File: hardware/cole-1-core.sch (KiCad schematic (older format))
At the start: 11 parts, among them SW1 SW_Push, U1 WD65C02, U2 ECS-100AX-2.0, U3 MAX1232CPA, U4 AT28C256-15PU, U5 CY62256NLL-70PXC

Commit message: - Change WE on the EEPROM to be tied to ground, like it is on the breadboard prototype. - Change TD pin on the MAX1232 to bre tied to Vcc, which raises the watchdog timeout to 1.2s. - Add Vcc and GND pins to each of the GPIO headers
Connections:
- wire segments 119 -> 121
- no-connect marks 7 -> 6
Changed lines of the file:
@@
 	9250 2150 9450 2150
-Wire Wire Line
-	4850 5150 9800 5150
 Wire Wire Line
 	4750 5250 9800 5250
@@
 	9800 800  9800 2200
 Wire Wire Line
-	5050 2750 4850 2750
-Wire Wire Line
-	4850 2750 4850 5150
+	4400 2750 5050 2750
 Wire Wire Line
 	4750 5250 4750 2850
@@
 Wire Wire Line
 	9450 2150 9450 5150
-Connection ~ 9450 5150
 Wire Wire Line
 	9250 2050 9350 2050
@@
 	4800 5550 4800 7000
 Connection ~ 3600 7000
-NoConn ~ 1850 7000
 Entry Wire Line
 	2700 2700 2800 2600
@@
 Entry Wire Line
 	2700 2300 2800 2200
+$Comp
+L VCC #PWR05
+U 1 1 5A514B68
+P 1700 6650
+F 0 "#PWR05" H 1700 6500 50  0001 C CNN
+F 1 "VCC" H 1700 6800 50  0000 C CNN
+F 2 "" H 1700 6650 50  0001 C CNN
+F 3 "" H 1700 6650 50  0001 C CNN
+	1    1700 6650
+	1    0    0    -1
+$EndComp
+Wire Wire Line
+	1850 7000 1700 7000
+Wire Wire Line
+	1700 7000 1700 6650
+$Comp
+L VCC #PWR06
+U 1 1 5A514D73
+P 4400 2400
+F 0 "#PWR06" H 4400 2250 50  0001 C CNN
+F 1 "VCC" H 4400 2550 50  0000 C CNN
+F 2 "" H 4400 2400 50  0001 C CNN
+F 3 "" H 4400 2400 50  0001 C CNN
+	1    4400 2400
+	1    0    0    -1
+$EndComp
+Wire Wire Line
+	4400 2400 4400 2750
+Wire Wire Line
+	9450 5150 9800 5150
 $EndSCHEMATC

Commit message: switch to a DIP-8 oscillator, and fix footprint for MAX1232
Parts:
- U2: value ECS-100AX-2.0 -> ECS-2100AX-2.0MHZ; footprint Housings_DIP:DIP-14_W7.62mm_Socket_LongPads -> Housings_DIP:DIP-8_W7.62mm_Socket_LongPads; symbol Osc_14pin -> Osc_8pin
- U3: footprint Housings_DIP:DIP-14_W7.62mm_Socket_LongPads -> Housings_DIP:DIP-8_W7.62mm_Socket_LongPads
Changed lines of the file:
@@
 F 0 "U3" H 2450 7350 60  0000 L BNN
 F 1 "MAX1232CPA" H 2200 6700 60  0000 L BNN
-F 2 "Housings_DIP:DIP-14_W7.62mm_Socket_LongPads" H 2600 7900 50  0001 L BNN
+F 2 "Housings_DIP:DIP-8_W7.62mm_Socket_LongPads" H 2600 7900 50  0001 L BNN
 F 3 "Maxim Integrated" H 2750 8100 50  0001 L BNN
 	1    2500 7050
@@
 	2700 2800 2700 5050
 $Comp
-L Osc_14pin U2
+L Osc_8pin U2
 U 1 1 5A43653F
 P 1900 4150
 F 0 "U2" H 1900 4450 60  0000 C CNN
-F 1 "ECS-100AX-2.0" H 1950 3850 60  0000 C CNN
-F 2 "Housings_DIP:DIP-14_W7.62mm_Socket_LongPads" H 1900 4150 60  0001 C CNN
+F 1 "ECS-2100AX-2.0MHZ" H 1950 3850 60  0000 C CNN
+F 2 "Housings_DIP:DIP-8_W7.62mm_Socket_LongPads" H 1900 4150 60  0001 C CNN
 F 3 "" H 1900 4150 60  0001 C CNN
 	1    1900 4150

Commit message: Final schematic and PCB layout.
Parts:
- R1, R2, R3, R4, R6: footprint Resistors_THT:R_Axial_DIN0207_L6.3mm_D2.5mm_P10.16mm_Horizontal -> Resistors_SMD:R_0805_HandSoldering
- U1: footprint Housings_DIP:DIP-40_W15.24mm_Socket_LongPads -> Housings_DIP:DIP-40_W15.24mm_Socket
- U2, U3: footprint Housings_DIP:DIP-8_W7.62mm_Socket_LongPads -> Housings_DIP:DIP-8_W7.62mm_Socket
- U4, U5: footprint Housings_DIP:DIP-28_W15.24mm_Socket_LongPads -> Housings_DIP:DIP-28_W15.24mm_Socket
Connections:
- net WATCHDOG is gone; now on net PHI2: U3.7 (*ST)
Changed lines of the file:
@@
 F 0 "U1" H 1900 3150 60  0000 C CNN
 F 1 "WD65C02" H 1900 950 60  0000 C CNN
-F 2 "Housings_DIP:DIP-40_W15.24mm_Socket_LongPads" H 1350 2300 60  0001 C CNN
+F 2 "Housings_DIP:DIP-40_W15.24mm_Socket" H 1350 2300 60  0001 C CNN
 F 3 "" H 1350 2300 60  0000 C CNN
 	1    1900 2100
@@
 F 0 "R4" V 700 2850 50  0000 L CNN
 F 1 "3.3K" V 800 2850 30  0000 L CNN
-F 2 "Resistors_THT:R_Axial_DIN0207_L6.3mm_D2.5mm_P10.16mm_Horizontal" H 800 2900 50  0001 C CNN
+F 2 "Resistors_SMD:R_0805_HandSoldering" H 800 2900 50  0001 C CNN
 F 3 "" H 800 2900 50  0001 C CNN
 	1    800  2900
@@
 F 0 "R1" V 700 2150 50  0000 L CNN
 F 1 "3.3K" V 800 2150 30  0000 L CNN
-F 2 "Resistors_THT:R_Axial_DIN0207_L6.3mm_D2.5mm_P10.16mm_Horizontal" H 800 2200 50  0001 C CNN
+F 2 "Resistors_SMD:R_0805_HandSoldering" H 800 2200 50  0001 C CNN
 F 3 "" H 800 2200 50  0001 C CNN
 	1    800  2200
@@
 F 0 "R3" V 700 2550 50  0000 L CNN
 F 1 "3.3K" V 800 2550 30  0000 L CNN
-F 2 "Resistors_THT:R_Axial_DIN0207_L6.3mm_D2.5mm_P10.16mm_Horizontal" H 800 2600 50  0001 C CNN
+F 2 "Resistors_SMD:R_0805_HandSoldering" H 800 2600 50  0001 C CNN
 F 3 "" H 800 2600 50  0001 C CNN
 	1    800  2600
@@
 F 0 "R2" V 700 2350 50  0000 L CNN
 F 1 "3.3K" V 800 2350 30  0000 L CNN
-F 2 "Resistors_THT:R_Axial_DIN0207_L6.3mm_D2.5mm_P10.16mm_Horizontal" H 800 2400 50  0001 C CNN
+F 2 "Resistors_SMD:R_0805_HandSoldering" H 800 2400 50  0001 C CNN
 F 3 "" H 800 2400 50  0001 C CNN
 	1    800  2400
@@
 F 0 "R6" H 3450 2650 50  0000 L CNN
 F 1 "10k" H 3550 2600 30  0000 L CNN
-F 2 "Resistors_THT:R_Axial_DIN0207_L6.3mm_D2.5mm_P10.16mm_Horizontal" H 3600 2600 50  0001 C CNN
+F 2 "Resistors_SMD:R_0805_HandSoldering" H 3600 2600 50  0001 C CNN
 F 3 "" H 3600 2600 50  0001 C CNN
 	1    3600 2600
@@
 F 0 "U4" H 5750 3050 60  0000 C CNN
 F 1 "AT28C256-15PU" H 5750 1000 60  0000 C CNN
-F 2 "Housings_DIP:DIP-28_W15.24mm_Socket_LongPads" H 5750 2050 50  0001 C CNN
+F 2 "Housings_DIP:DIP-28_W15.24mm_Socket" H 5750 2050 50  0001 C CNN
 F 3 "" H 5750 2050 50  0001 C CNN
 	1    5750 2050
@@
 F 0 "U5" H 8750 2900 60  0000 C CNN
 F 1 "CY62256NLL-70PXC" H 8750 1100 60  0000 C CNN
-F 2 "Housings_DIP:DIP-28_W15.24mm_Socket_LongPads" H 8750 1950 50  0001 C CIN
+F 2 "Housings_DIP:DIP-28_W15.24mm_Socket" H 8750 1950 50  0001 C CIN
 F 3 "" H 8750 1950 50  0001 C CNN
 	1    8750 1950
@@
 F 0 "U3" H 2450 7350 60  0000 L BNN
 F 1 "MAX1232CPA" H 2200 6700 60  0000 L BNN
-F 2 "Housings_DIP:DIP-8_W7.62mm_Socket_LongPads" H 2600 7900 50  0001 L BNN
+F 2 "Housings_DIP:DIP-8_W7.62mm_Socket" H 2600 7900 50  0001 L BNN
 F 3 "Maxim Integrated" H 2750 8100 50  0001 L BNN
 	1    2500 7050
@@
 Text HLabel 9850 5550 2    60   Output ~ 0
 RESET
-Text HLabel 9800 5450 2    60   Input ~ 0
-WATCHDOG
 Connection ~ 3600 3100
 Wire Wire Line
@@
 F 0 "U2" H 1900 4450 60  0000 C CNN
 F 1 "ECS-2100AX-2.0MHZ" H 1950 3850 60  0000 C CNN
-F 2 "Housings_DIP:DIP-8_W7.62mm_Socket_LongPads" H 1900 4150 60  0001 C CNN
+F 2 "Housings_DIP:DIP-8_W7.62mm_Socket" H 1900 4150 60  0001 C CNN
 F 3 "" H 1900 4150 60  0001 C CNN
 	1    1900 4150
@@
 	3150 7000 4800 7000
 NoConn ~ 3150 7100
-Wire Wire Line
-	9800 5450 4650 5450
-Wire Wire Line
-	4650 5450 4650 6900
-Wire Wire Line
-	4650 6900 3150 6900
 Wire Wire Line
 	9850 5550 4800 5550
@@
 Wire Wire Line
 	9450 5150 9800 5150
+Wire Wire Line
+	3150 6900 3500 6900
+Wire Wire Line
+	3500 6900 3500 5050
+Connection ~ 3500 5050
 $EndSCHEMATC

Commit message: Updated schematics, board layout, and GAL code for COLE-1+
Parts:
- added R6: 3.3K, Resistor_SMD:R_0805_2012Metric_Pad1.15x1.40mm_HandSolder, symbol cole-1-rescue:R_Small
- added U5: WD65C22, Package_DIP:DIP-40_W15.24mm_Socket, symbol 65xx:W65C22SxP
- added U7: MC68B50, Package_DIP:DIP-24_W15.24mm_Socket, symbol Interface_UART:MC6850
- added U8: CGL, Package_DIP:DIP-24_W7.62mm_Socket, symbol gal:CGL
- R1, R2, R3, R4: footprint Resistors_SMD:R_0805_HandSoldering -> Resistor_SMD:R_0805_2012Metric_Pad1.15x1.40mm_HandSolder; symbol R_Small -> cole-1-rescue:R_Small
- R5: renamed from R6; footprint Resistors_SMD:R_0805_HandSoldering -> Resistor_SMD:R_0805_2012Metric_Pad1.15x1.40mm_HandSolder; symbol R_Small -> cole-1-rescue:R_Small
- SW1: footprint Buttons_Switches_THT:SW_PUSH_6mm -> Button_Switch_THT:SW_PUSH_6mm_H5mm; symbol SW_Push -> cole-1-rescue:SW_Push
- U1: renamed from U2; value ECS-2100AX-2.0MHZ -> EC11TS-3.6864M; footprint Housings_DIP:DIP-8_W7.62mm_Socket -> Package_DIP:DIP-8_W7.62mm_Socket; symbol Osc_8pin -> osc:Osc_8pin
- U2: renamed from U1; value WD65C02 -> W65C816; footprint Housings_DIP:DIP-40_W15.24mm_Socket -> Package_DIP:DIP-40_W15.24mm_Socket; symbol WD65C02_ -> 65xx:W65C816SxP
- U3: footprint Housings_DIP:DIP-8_W7.62mm_Socket -> Package_DIP:DIP-8_W7.62mm_Socket; symbol MAX1232CPA -> MAX1232:MAX1232CPA
- U4: footprint Housings_DIP:DIP-28_W15.24mm_Socket -> Package_DIP:DIP-28_W15.24mm_Socket; symbol 28C256 -> Memory_RAM:CY62256-70PC
- U6: renamed from U5; footprint Housings_DIP:DIP-28_W15.24mm_Socket -> Package_DIP:DIP-28_W15.24mm_Socket; symbol HM62256BLP-7 -> Memory_RAM:CY62256-70PC
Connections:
- net A0: now also U5.38 (RS0), U7.11 (RS)
- net A1: now also U5.37 (RS1)
- net A12: now also U8.7 (A11)
- net A13: now also U8.8 (A12)
- net A14: now also U8.9 (A13)
- net A15: now also U8.10 (A14); no longer U6.20 (~CS)
- net A2: now also U5.36 (RS2)
- net A3: now also U5.35 (RS3)
- net A4: now also U8.6 (A10)
- net D0: now also U5.33 (D0), U7.22 (D0)
- net D1: now also U5.32 (D1), U7.21 (D1)
- net D2: now also U5.31 (D2), U7.20 (D2)
- net D3: now also U5.30 (D3), U7.19 (D3)
- net D4: now also U5.29 (D4), U7.18 (D4)
- net D5: now also U5.28 (D5), U7.17 (D5)
- net D6: now also U5.27 (D6), U7.16 (D6)
- net D7: now also U5.26 (D7), U7.15 (D7)
- net GND: now also U5.1 (VSS), U7.1 (VSS), U7.23 (~DCD), U8.12 (GND)
- net PHI2: now also U5.25 (ϕ2), U7.14 (E), U7.3 (Rx_CLK), U7.4 (Tx_CLK), U8.2 (R~W)
- net VCC: now also R6.2, U5.20 (VCC), U5.24 (CS1), U7.10 (CS1), U7.12 (VCC), U7.8 (CS0), U8.24 (VCC); no longer U4.27 (WE)
- net at U2.2 (RDY): now also R3.1; no longer R1.1
- net at U2.3 (~ABORT): now also R1.1
- net at U2.36 (BE): now also R4.1; no longer R2.1
- net at U2.38 (MX): no longer R3.1
- net at U2.6 (~NMI): now also R2.1; no longer R4.1
- net IRQ renamed ~IRQ
- net ~IRQ: now also U8.17 (~IRQ)
- net RD renamed ~RD
- net ~RD: now also U8.15 (~RD)
- net RESET renamed ~RESET
- net ~RESET: now also U5.34 (~RES)
- net ROMSEL renamed ~ROMSEL
- net ~ROMSEL: now also U8.21 (~ROMSEL)
- net RWB renamed R~W
- net R~W: now also U5.22 (R/~W), U7.13 (R/~W), U8.3 (~UARTIRQ)
- net WR renamed ~WR
- net ~WR: now also U4.27 (~WE), U8.16 (~WR)
- new net CA1: U5.40 (CA1)
- new net CA2: U5.39 (CA2)
- new net CB1: U5.18 (CB1)
- new net CB2: U5.19 (CB2)
- new net CTS: U7.24 (~CTS)
- new net PA0: U5.2 (PA0)
- new net PA1: U5.3 (PA1)
- new net PA2: U5.4 (PA2)
- new net PA3: U5.5 (PA3)
- new net PA4: U5.6 (PA4)
- new net PA5: U5.7 (PA5)
- new net PA6: U5.8 (PA6)
- new net PA7: U5.9 (PA7)
- new net PB0: U5.10 (PB0)
- new net PB1: U5.11 (PB1)
- new net PB2: U5.12 (PB2)
- new net PB3: U5.13 (PB3)
- new net PB4: U5.14 (PB4)
- new net PB5: U5.15 (PB5)
- new net PB6: U5.16 (PB6)
- new net PB7: U5.17 (PB7)
- new net RTS: U7.5 (~RTS)
- new net RXD: U7.2 (Rx_Data)
- new net TXD: U7.6 (Tx_Data)
- new net ~RAMSEL: U6.20 (~CS), U8.20 (~RAMSEL)
- new net ~UARTIRQ: R6.1, U7.7 (~IRQ), U8.4 (~VIAIRQ)
- new net ~UARTSEL: U7.9 (CS2), U8.18 (~UARTSEL)
- new net ~VIAIRQ: U5.21 (~IRQ), U8.5 (A4)
- new net ~VIASEL: U5.23 (~CS2), U8.19 (~VIASEL)
- no-connect marks 6 -> 7
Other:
- moved on the sheet: R1, R2, R3, R4, R5, SW1

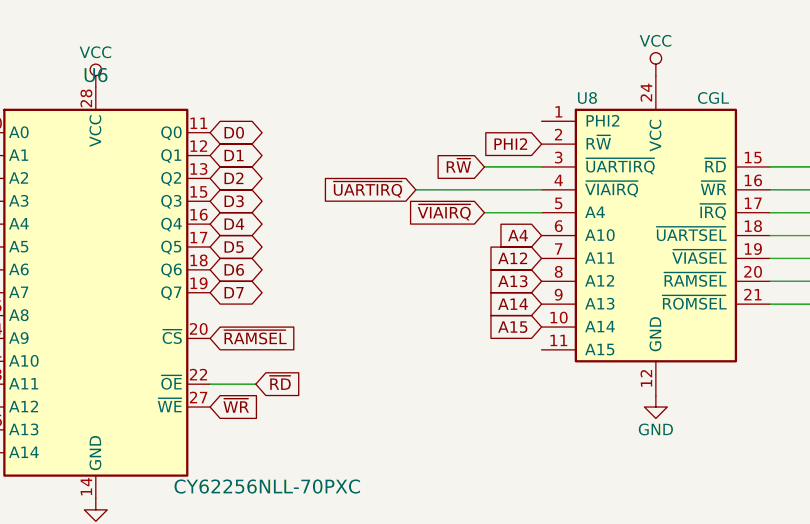
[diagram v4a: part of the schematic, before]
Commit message: Add A10 and A11 routing to GAL, and update GAL equations
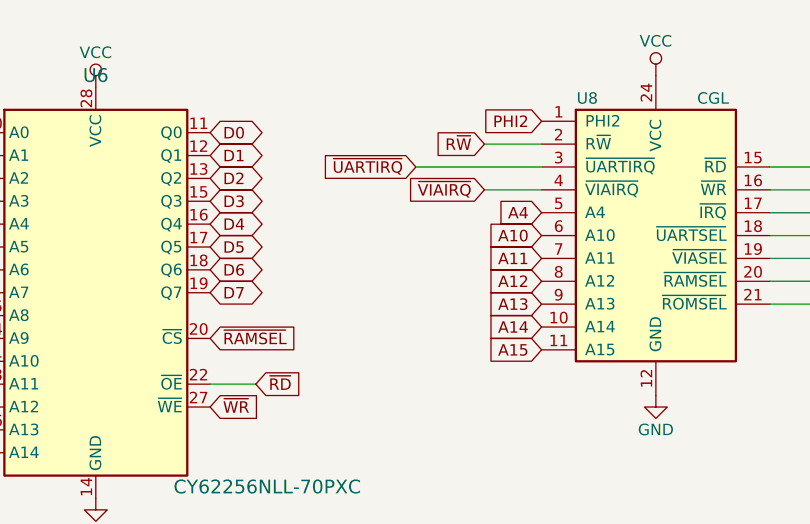
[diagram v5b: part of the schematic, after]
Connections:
- net A10: now also U8.6 (A10)
- net A11: now also U8.7 (A11)
- net A12: now also U8.8 (A12); no longer U8.7 (A11)
- net A13: now also U8.9 (A13); no longer U8.8 (A12)
- net A14: now also U8.10 (A14); no longer U8.9 (A13)
- net A15: now also U8.11 (A15); no longer U8.10 (A14)
- net A4: now also U8.5 (A4); no longer U8.6 (A10)
- net PHI2: now also U8.1 (PHI2); no longer U8.2 (R~W)
- net R~W: now also U8.2 (R~W); no longer U8.3 (~UARTIRQ)
- net ~UARTIRQ: now also U8.3 (~UARTIRQ); no longer U8.4 (~VIAIRQ)
- net ~VIAIRQ: now also U8.4 (~VIAIRQ); no longer U8.5 (A4)
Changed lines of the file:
@@
 ~IRQ
 Wire Wire Line
-	8300 1500 8050 1500
-Text GLabel 8050 1500 0    50   Input ~ 0
+	8300 1400 8050 1400
+Text GLabel 8050 1400 0    50   Input ~ 0
 ~VIAIRQ
 Wire Wire Line
-	8300 1400 7750 1400
-Text GLabel 7750 1400 0    50   Input ~ 0
+	8300 1300 7750 1300
+Text GLabel 7750 1300 0    50   Input ~ 0
 ~UARTIRQ
 Wire Wire Line
-	8300 1300 8050 1300
-Text GLabel 8050 1300 0    50   Input ~ 0
+	8300 1200 8050 1200
+Text GLabel 8050 1200 0    50   Input ~ 0
 R~W
-Text GLabel 8300 1200 0    50   Input ~ 0
+Text GLabel 8300 1100 0    50   Input ~ 0
 PHI2
+Text GLabel 8300 2100 0    50   Input ~ 0
+A15
 Text GLabel 8300 2000 0    50   Input ~ 0
-A15
+A14
 Text GLabel 8300 1900 0    50   Input ~ 0
-A14
+A13
 Text GLabel 8300 1800 0    50   Input ~ 0
-A13
-Text GLabel 8300 1700 0    50   Input ~ 0
 A12
-Text GLabel 8300 1600 0    50   Input ~ 0
+Text GLabel 8300 1500 0    50   Input ~ 0
 A4
 $Comp
@@
 Wire Wire Line
 	8200 3300 8200 3400
+Text GLabel 8300 1600 0    50   Input ~ 0
+A10
+Text GLabel 8300 1700 0    50   Input ~ 0
+A11
 $EndSCHEMATC
